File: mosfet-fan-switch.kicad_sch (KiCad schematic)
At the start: 21 parts, among them J1 12V IN, J2 PWM IN, J3 FAN OUT, Q1 irfz44n, Q2 2n7002, Q3 irf7416, U1 Arduino_Pro_Mini_3V3

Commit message: schematic + sim: NUC fan-header interface (PWM request divider, tach answer)
- J2 grown to 1x04 (Pro Mini), J4 added as the NUC's own 4-pin fan socket
- R7/R8 divider 10k/10k takes the NUC's 5 V PWM request down to the 3.3 V the
  Pro Mini expects; C5 1u + C6 100n filter it (tau 5.49 ms)
- R9 1k + Q4 (BC547) answer on the tach line as an open collector; the pull-up
  lives in the NUC (V4 + R10, both DNP)
- sim-only stand-ins V3/V4/V5, all DNP; connectors excluded from simulation
- fixed a pre-existing wiring bug: the old V2 -> R1 /PWM wire ran down U1's pin
  column and shorted D10-D13 to /PWM.  /PWM is D9 only.
- sim/nuc_link.py: duty table (2.500 V tap, 775 counts at 100 %, <=5 mV ripple),
  250 uA ITE load, tach levels, the legal 23-350 Hz carrier window
- sim/models/bc547.lib added and wired into the variant decks
- tools/fix_schematic_junctions.py restores junction dots that the KiCad MCP
  schematic edits silently delete
ERC: 0 errors, 0 warnings
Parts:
- removed J2: PWM IN, Connector_PinHeader_2.54mm:PinHeader_1x02_P2.54mm_Vertical, symbol Connector:Conn_01x02_Pin
- added C5: 1u, Capacitor_THT:CP_Radial_D8.0mm_P3.50mm, symbol Device:C
- added C6: 100n, Capacitor_THT:C_Disc_D3.8mm_W2.6mm_P2.50mm, symbol Device:C
- added J2: PRO MINI, Connector_PinHeader_2.54mm:PinHeader_1x04_P2.54mm_Vertical, symbol Connector_Generic:Conn_01x04
- added J4: NUC FAN HEADER, Connector_PinHeader_2.54mm:PinHeader_1x04_P2.54mm_Vertical, symbol Connector_Generic:Conn_01x04
- added Q4: BC547, Package_TO_SOT_THT:TO-92_Inline_Wide, symbol Transistor_BJT:BC547
- added R10: 1k, symbol Device:R
- added R7, R8: 10k, Resistor_THT:R_Axial_DIN0207_L6.3mm_D2.5mm_P7.62mm_Horizontal, symbol Device:R
- added R9: 1k, Resistor_THT:R_Axial_DIN0207_L6.3mm_D2.5mm_P7.62mm_Horizontal, symbol Device:R
- added V3, V5: VPULSE, symbol Simulation_SPICE:VPULSE
- added V4: 5, symbol Simulation_SPICE:VDC
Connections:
- net GND: now also C5.2, C6.2, J2.2 (Pin_2), J4.4 (Pin_4), Q4.3 (E), R8.2, V3.2, V4.2, V5.2
- net PWM: now also J2.1 (Pin_1)
- net TACH_PWM: now reaches U1.13 (D10)
- net TACH_PWM: now also J2.4 (Pin_4), R9.1, V5.1
- net DEMAND: now reaches U1.19 (A0)
- net DEMAND: now also C5.1, C6.1, J2.3 (Pin_3), R7.2, R8.1
- new net NUC_PWM: J4.1 (Pin_1), R7.1, V3.1
- new net NUC_TACH: J4.2 (Pin_2), Q4.1 (C), R10.1
- new net P5V: R10.2, V4.1
- new net TBASE: Q4.2 (B), R9.2
- no-connect marks 27 -> 26

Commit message: schematic: package-accurate transistor symbols; board stripped to a routing skeleton
The four transistors are now symbols whose pin numbers are the real leg numbers, so
KiCad's "symbol pin N <-> footprint pad N" rule puts every net on the correct leg and
Update PCB from Schematic agrees with the layout instead of fighting it.

- mosfet-fan-switch.kicad_sym + sym-lib-table: Q_NMOS_TO220 (1 gate, 2 drain, 3
  source), Q_NMOS_SOT23 (1 gate, 2 source, 3 drain), Q_PMOS_SO8 (1-3 source, 4 gate,
  5-8 drain), Q_NPN_TO92 (1 emitter, 2 base, 3 collector).  KiCad ships nothing like
  these: Transistor_BJT:BC547 extends Q_NPN_CBE (wrong for the flat-face TO-92) and
  there is no IRFZ44N symbol in any library at all.
- KiCad 10 ignores Sim.Pins for .model cards and writes every device line in symbol
  pin order, so the ngspice terminal order moved into .subckt wrappers in
  sim/models/*.lib:  XQ1 /GATE /DRAIN GND mos_irfz44n, XQ2 /LGATE GND /BOOT
  mos_2n7002, XQ3 /P12V x3 /BOOT /HIGATE x4 mos_irf7416, XQ4 GND /TBASE /NUC_TACH
  npn_bc547.  ngspice wants four nodes on a MOSFET card, so the bulk is spelled out
  and tied to the source inside each wrapper.
- sim/prepare_deck.py no longer repairs the NC-Q2-0 floating bulk (the three-pin
  SPICE symbols are gone); sim/variants.py and sim/nuc_link.py key the X cards and
  the pass-transistor variants now list nets in the chosen wrapper's own order.
  variants.csv is byte-identical to the pre-change baseline; fan_count.csv and
  nuc_link.csv differ only in timestep-sensitive averaged columns (supply average
  186.8 -> 187.2 mA, ITE load 40.3 -> 40.9 uA) - every DC and peak value identical.
- Q3 is drawn as the 8-pin package box, its legs tied by segmented wires with each
  node labelled once, moved east to (189.23, 170.18) so the 9.53 mm body clears the
  /BOOT branch at x=177.8.  ERC: 0 errors, 0 warnings.
- board: tools/skeleton_board.py removed the 63 generated tracks and kept all 26
  footprints, their positions and every pad's n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
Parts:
- Q1: symbol Simulation_SPICE:NMOS_Substrate -> mosfet-fan-switch:Q_NMOS_TO220
- Q2: symbol Simulation_SPICE:NMOS -> mosfet-fan-switch:Q_NMOS_SOT23
- Q3: symbol Simulation_SPICE:PMOS_Substrate -> mosfet-fan-switch:Q_PMOS_SO8
- Q4: symbol Transistor_BJT:BC547 -> mosfet-fan-switch:Q_NPN_TO92
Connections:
- net BOOT: now also Q2.3 (D), Q3.4 (G); no longer Q2.1 (D), Q3.2 (G)
- net DRAIN: now also Q1.2 (D); no longer Q1.1 (D)
- net GATE: now also Q1.1 (G); no longer Q1.2 (G)
- net GND: now also Q2.2 (S), Q4.1 (E); no longer Q1.4 (Bulk), Q2.3 (S), Q4.3 (E)
- net HIGATE: now also Q3.5 (D), Q3.6 (D), Q3.7 (D), Q3.8 (D); no longer Q3.1 (D)
- net LGATE: now also Q2.1 (G); no longer Q2.2 (G)
- net NUC_TACH: now also Q4.3 (C); no longer Q4.1 (C)
- net P12V: now also Q3.1 (S), Q3.2 (S); no longer Q3.4 (Bulk)
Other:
- note added: "PHYSICAL PINOUTS - symbols use package pin order: sheet numbers = board legs Q2 2N7002 SOT-23 1 gate /LGATE 2 source /GND 3 drain /BOOT Q3 IRF7416 SO-8 1,2,3 source /P12V 4 gate /BOOT 5..8 drain /HIGATE Q1 IRFZ44N TO-220 1 gate /GATE 2 drain /DRAIN 3 source /GND Q4 BC547 TO-92 1 emitter /GND 2 base /TBASE 3 collector /NUC_TACH D1 1N5819 DO-41 banded end (cathode) to +12 V, other end to /DRAIN J3 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"
- note removed: "PHYSICAL PINOUTS - the board follows the package, not the symbol's pin order Q2 2N7002 SOT-23 1 gate /LGATE 2 source /GND 3 drain /BOOT Q3 IRF7416 SO-8 1,2,3 source /P12V 4 gate /BOOT 5..8 drain /HIGATE Q1 IRFZ44N TO-220 1 gate /GATE 2 drain /DRAIN 3 source /GND D1 1N5819 DO-41 banded end (cathode) to +12 V, other end to /DRAIN J3 3 fans odd pins = +12 V, even pins = the switched /DRAIN side The 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"
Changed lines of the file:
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@@
 	)
 	(symbol
-		(lib_id "Simulation_SPICE:NMOS")
+		(lib_id "mosfet-fan-switch:Q_NMOS_SOT23")
 		(at 143.51 170.18 0)
 		(unit 1)
@@
 			)
 		)
-		(property "Sim.Name" "2n7002"
-			(at 143.51 170.18 0)
-			(effects
-				(font
-					(size 1.27 1.27)
-				)
-				(hide yes)
-			)
-		)
-		(property "Sim.Type" "VDMOS"
+		(property "Sim.Name" "mos_2n7002"
 			(at 143.51 170.18 0)
 			(effects
@@
 	)
 	(symbol
-		(lib_id "Simulation_SPICE:PMOS_Substrate")
-		(at 184.15 170.18 180)
+		(lib_id "mosfet-fan-switch:Q_PMOS_SO8")
+		(at 189.23 170.18 0)
 		(unit 1)
 		(body_style 1)
@@
 		(dnp no)
 		(property "Reference" "Q3"
-			(at 177.8 168.91 0)
+			(at 181.61 163.5 0)
 			(show_name no)
 			(do_not_autoplace no)
@@
 		)
 		(property "Value" "irf7416"
-			(at 177.8 171.45 0)
+			(at 186.69 177.8 0)
 			(show_name no)
 			(do_not_autoplace no)
@@
 		)
 		(property "Description" "P-channel MOSFET symbol with substrate (bulk) pin"
-			(at 184.15 170.18 0)
+			(at 189.23 170.18 0)
 			(hide yes)
 			(show_name no)
@@
 		)
 		(property "Sim.Library" "sim/models/irf7416.lib"
-			(at 184.15 170.18 0)
+			(at 189.23 170.18 0)
 			(effects
 				(font
@@
 			)
 		)
-		(property "Sim.Name" "irf7416"
-			(at 184.15 170.18 0)
-			(effects
-				(font
-					(size 1.27 1.27)
-				)
-				(hide yes)
-			)
-		)
-		(property "Sim.Type" "VDMOS"
-			(at 184.15 170.18 0)
+		(property "Sim.Name" "mos_irf7416"
+			(at 189.23 170.18 0)
 			(effects
 				(font
@@
 		(pin "4"
 		)
+		(pin "5"
+		)
+		(pin "6"
+		)
+		(pin "7"
+		)
+		(pin "8"
+		)
 		(instances
 			(project "mosfet-fan-switch"
@@
 	)
 	(symbol
-		(lib_id "Simulation_SPICE:NMOS_Substrate")
+		(lib_id "mosfet-fan-switch:Q_NMOS_TO220")
 		(at 224.79 190.5 0)
 		(unit 1)
@@
 			)
 		)
-		(property "Sim.Name" "irfz44n"
-			(at 224.79 190.5 0)
-			(effects
-				(font
-					(size 1.27 1.27)
-				)
-				(hide yes)
-			)
-		)
-		(property "Sim.Type" "VDMOS"
+		(property "Sim.Name" "mos_irfz44n"
 			(at 224.79 190.5 0)
 			(effects
@@
 		(pin "3"
 		)
-		(pin "4"
-		)
 		(instances
 			(project "mosfet-fan-switch"
@@
 	(wire
 		(pts
-			(xy 195.58 170.18) (xy 187.96 170.18)
+			(xy 195.58 170.18) (xy 193.04 170.18)
 		)
 		(stroke
@@
 	(wire
 		(pts
-			(xy 181.61 165.1) (xy 181.61 111.76)
-		)
-		(stroke
-			(width 0)
-			(type default)
-		)
-	)
-	(wire
-		(pts
-			(xy 179.07 165.1) (xy 181.61 165.1)
+			(xy 184.15 165.1) (xy 184.15 111.76)
 		)
 		(stroke
@@
 	(wire
 		(pts
-			(xy 227.32999999999998 195.58) (xy 229.87 195.58)
-		)
-		(stroke
-			(width 0)
-			(type default)
-		)
-	)
-	(wire
-		(pts
 			(xy 203.2 207.01) (xy 203.2 210.82)
 		)
@@
 	)
 	(label "BOOT"
-		(at 187.96 170.18 0)
-		(effects
-			(font
-				(size 1.27 1.27)
-			)
-			(justify left bottom)
-		)
-	)
-	(label "P12V"
-		(at 181.61 165.1 90)
+		(at 193.04 170.18 0)
 		(effects
 			(font
@@
 	)
 	(label "P12V"
-		(at 179.07 165.1 90)
+		(at 184.15 162.56 90)
 		(effects
 			(font
@@
 		)
 	)
-	(label "GND"
-		(at 229.87 195.58 270)
-		(effects
-			(font
-				(size 1.27 1.27)
-			)
-			(justify right bottom)
-		)
-	)
 	(label "P12V"
 		(at 241.3 148.59 90)
@@
 		)
 	)
-	(text "PHYSICAL PINOUTS - the board follows the package, not the symbol's pin order\nQ2  2N7002  SOT-23    1 gate /LGATE    2 source /GND     3 drain /BOOT\nQ3  IRF7416 SO-8      1,2,3 source /P12V   4 gate /BOOT   5..8 drain /HIGATE\nQ1  IRFZ44N TO-220    1 gate /GATE     2 drain /DRAIN    3 source /GND\nD1  1N5819  DO-41     banded end (cathode) to +12 V, other end to /DRAIN\nJ3  3 fans            odd pins = +12 V, even pins = the switched /DRAIN side\nThe SPICE symbols number MOSFET pins D-G-S, which is NOT the package order.\ndocs/pcb-notes.md carries the full pad-to-net table for the board."
+	(text "PHYSICAL PINOUTS - symbols use package pin order: sheet numbers = board legs\nQ2  2N7002  SOT-23    1 gate /LGATE    2 source /GND     3 drain /BOOT\nQ3  IRF7416 SO-8      1,2,3 source /P12V   4 gate /BOOT   5..8 drain /HIGATE\nQ1  IRFZ44N TO-220    1 gate /GATE     2 drain /DRAIN    3 source /GND\nQ4  BC547   TO-92     1 emitter /GND   2 base /TBASE     3 collector /NUC_TACH\nD1  1N5819  DO-41     banded end (cathode) to +12 V, other end to /DRAIN\nJ3  3 fans            odd pins = +12 V, even pins = the switched /DRAIN side\nngspice's own order (D-G-S-B, C-B-E) lives in the sim/models/ subckt wrappers\ndocs/pcb-notes.md carries the full pad-to-net table for the board."
 		(exclude_from_sim no)
 		(at 232 244 0)
@@
 	)
 	(junction
-		(at 138.43 170.18)
-		(diameter 0)
-		(color 0 0 0 0)
-	)
-	(junction
 		(at 138.43 210.82)
 		(diameter 0)
@@
 	)
 	(junction
-		(at 181.61 111.76)
-		(diameter 0)
-		(color 0 0 0 0)
-	)
-	(junction
-		(at 181.61 165.1)
+		(at 184.15 111.76)
 		(diameter 0)
 		(color 0 0 0 0)
@@
 	)
 	(junction
-		(at 227.33 195.58)
-		(diameter 0)
-		(color 0 0 0 0)
-	)
-	(junction
 		(at 227.33 210.82)
 		(diameter 0)
@@
 		(color 0 0 0 0)
 	)
-	(junction
-		(at 373.38 204.47)
-		(diameter 0)
-		(color 0 0 0 0)
-	)
 	(symbol
 		(lib_id "Simulation_SPICE:VPULSE")
@@
 	)
 	(symbol
-		(lib_id "Transistor_BJT:BC547")
+		(lib_id "mosfet-fan-switch:Q_NPN_TO92")
 		(at 378.46 204.47 0)
 		(unit 1)
@@
 			)
 		)
-		(property "Sim.Type" "GUMMELPOON"
-			(at 378.46 204.47 0)
-			(effects
-				(font
-					(size 1.27 1.27)
-				)
-				(hide yes)
-			)
-		)
-		(property "Sim.Name" "bc547"
+		(property "Sim.Name" "npn_bc547"
 			(at 378.46 204.47 0)
 			(effects
@@
 		)
 	)
+	(wire
+		(pts
+			(xy 184.15 165.1) (xy 186.69 165.1)
+		)
+		(stroke
+			(width 0)
+			(type default)
+		)
+	)
+	(wire
+		(pts
+			(xy 186.69 165.1) (xy 189.23 165.1)
+		)
+		(stroke
+			(width 0)
+			(type default)
+		)
+	)
+	(wire
+		(pts
+			(xy 181.61 175.26000000000002) (xy 184.15 175.26000000000002)
+		)
+		(stroke
+			(width 0)
+			(type default)
+		)
+	)
+	(wire
+		(pts
+			(xy 184.15 175.26000000000002) (xy 186.69 175.26000000000002)
+		)
+		(stroke
+			(width 0)
+			(type default)
+		)
+	)
+	(wire
+		(pts
+			(xy 186.69 175.26000000000002) (xy 189.23 175.26000000000002)
+		)
+		(stroke
+			(width 0)
+			(type default)
+		)
+	)

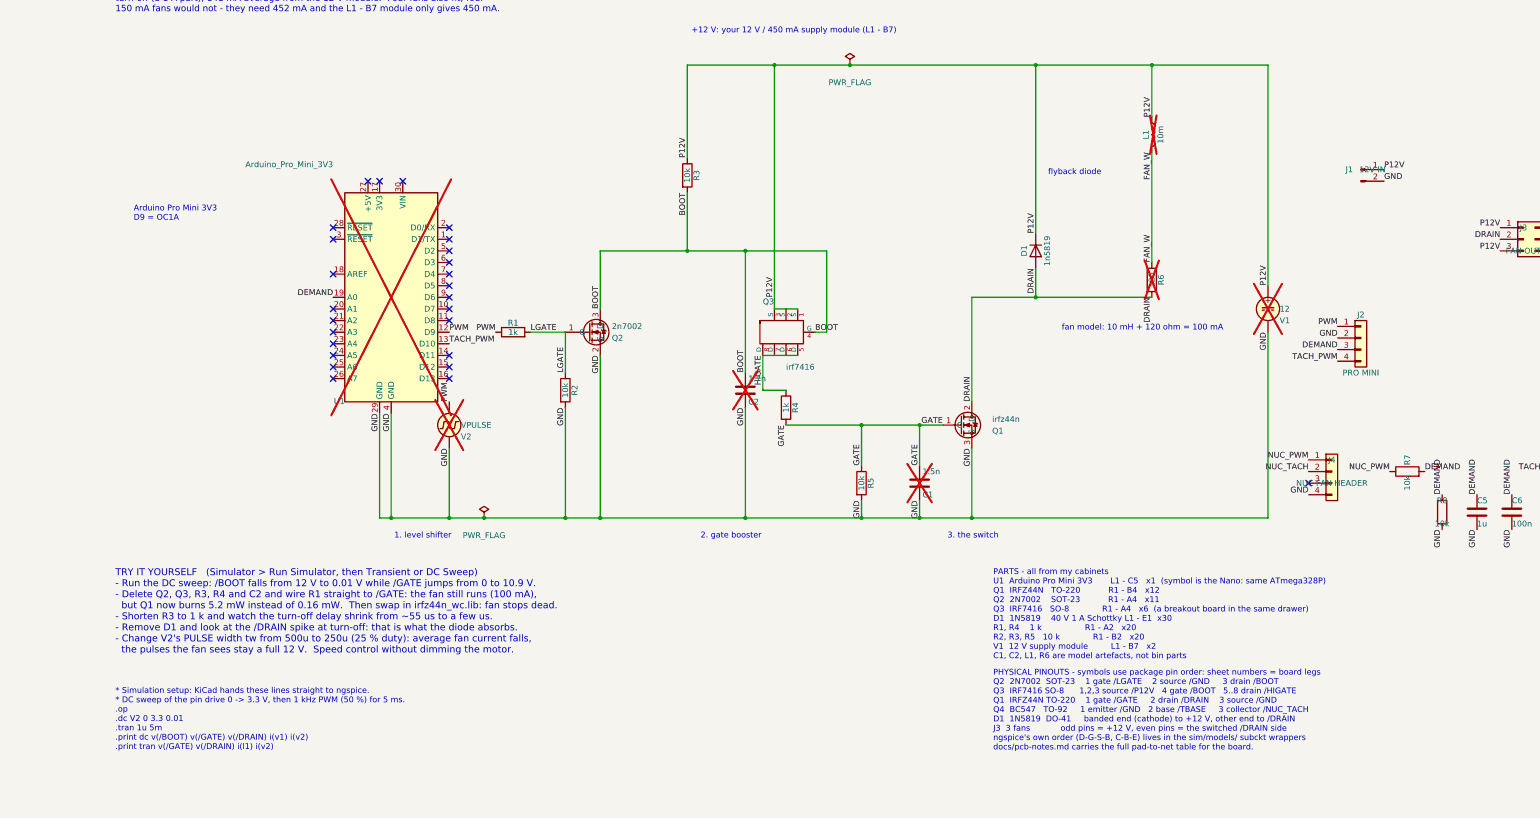
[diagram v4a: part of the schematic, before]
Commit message: sch: draw the Pro Mini itself, with its FTDI and ICSP headers
The Nano stand-in is gone.  U1 is now mosfet-fan-switch:Arduino_Pro_Mini_328,
generated from the same hole map as the board's socket footprint, so a symbol
pin number, a footprint pad number and the hole's silkscreen name are one
number.  J2 - the header that used to carry four signals to a module that was
not on the board - is deleted.

  * pcb/pro_mini.py now emits the symbol as well as the footprint.
  * tools/embed_pro_mini_schematic.py is the one-shot migration: it drops the
    Nano and J2 with their labels, no-connects and stubs, draws U1, J5 (FTDI
    row), J6 (2x3 ICSP, pin 2 deliberately dead), D2 and D3 (spare flyback
    diodes, unpopulated), and hands U1's programming-row GND to the GND rail.
  * KiCad only resolves symbols from the sheet's own lib_symbols cache, so the
    migration carries cached copies of everything it introduces.
  * Every new anchor sits on the 1.27 mm connection grid, which is what ERC's
    endpoint_off_grid check wants.
  * The board's footprints adopt the sheet's uuids, and D2/D3/J5/J6 now carry
    their real values.

ERC: 0 errors, 0 warnings.  DRC on the routing skeleton: no courtyard, silk,
clearance or hole violations; the same 7 cosmetic lib_footprint_mismatch
warnings and 68 expected unconnected pads.
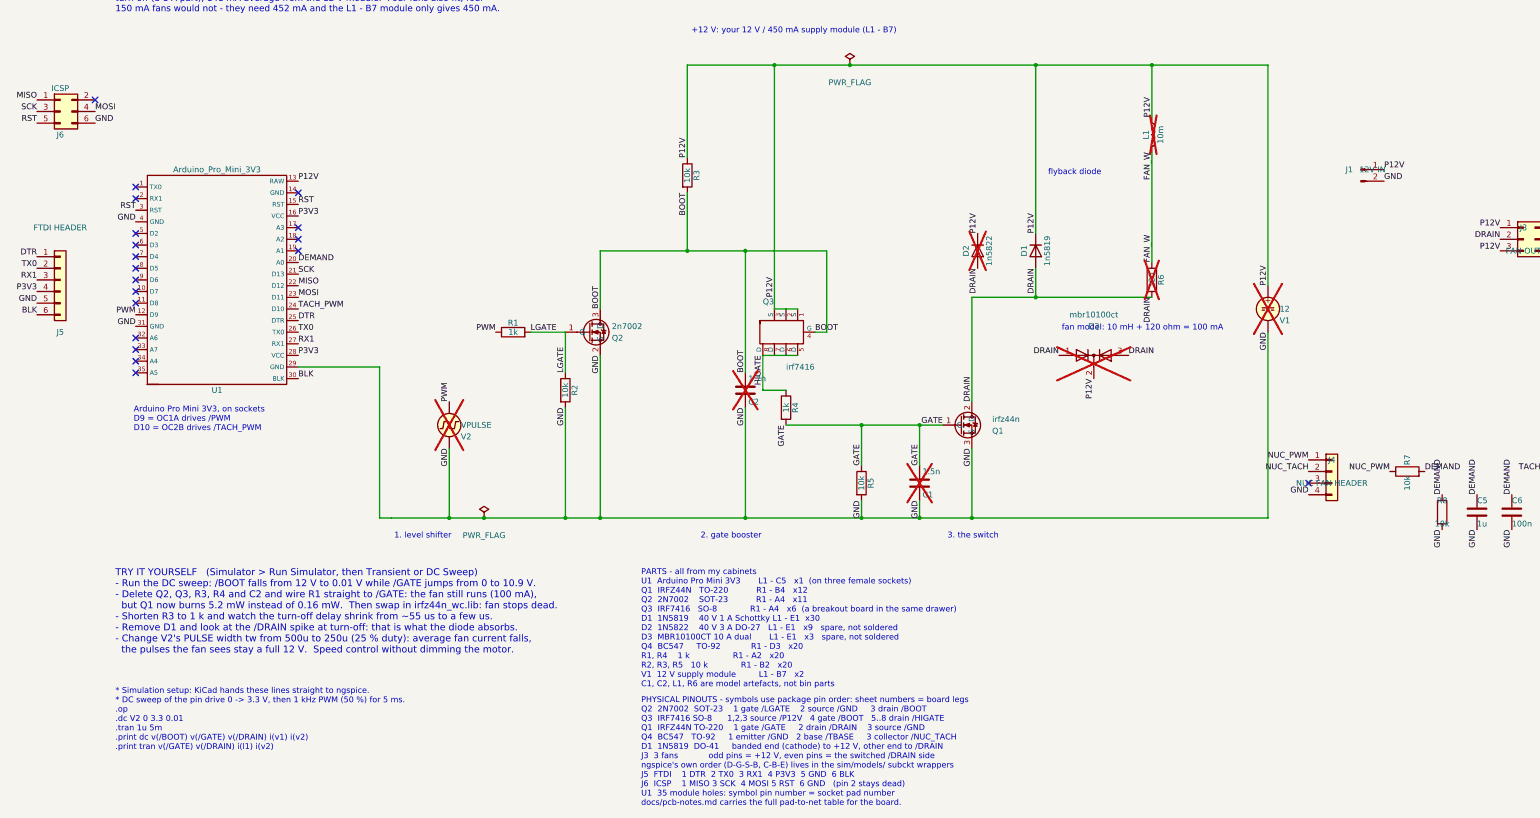
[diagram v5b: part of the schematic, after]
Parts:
- removed J2: PRO MINI, Connector_PinHeader_2.54mm:PinHeader_1x04_P2.54mm_Vertical, symbol Connector_Generic:Conn_01x04
- added D2: 1n5822, Diode_THT:D_DO-27_P15.24mm_Horizontal, symbol Device:D
- added D3: mbr10100ct, Package_TO_SOT_THT:TO-220-3_Vertical, symbol Device:D_Dual_CommonCathode_AKA
- added J5: FTDI HEADER, Connector_PinHeader_2.54mm:PinHeader_1x06_P2.54mm_Vertical, symbol Connector_Generic:Conn_01x06
- added J6: ICSP, Connector_PinHeader_2.54mm:PinHeader_2x03_P2.54mm_Vertical, symbol Connector_Generic:Conn_02x03_Odd_Even
- U1: footprint (none) -> mosfet-fan-switch:Arduino_Pro_Mini_328_Socket; symbol MCU_Module:Arduino_Nano_v2.x -> mosfet-fan-switch:Arduino_Pro_Mini_328; Note (none) -> the module sits on three female headers; measure its row sp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; now fitted
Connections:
- net DEMAND: now also U1.20 (A0); no longer U1.19 (A0)
- net DRAIN: now also D2.2 (A), D3.1 (A), D3.3 (A)
- net GND: now also U1.31 (GND), J5.5 (Pin_5), J6.6 (Pin_6)
- net P12V: now also U1.13 (RAW), D2.1 (K), D3.2 (K)
- net TACH_PWM: now also U1.24 (D10); no longer U1.13 (D10)
- net RST: now reaches U1.15 (RST)
- net RST: now also U1.3 (RST), J6.5 (Pin_5)
- net P3V3: now reaches U1.16 (VCC)
- net P3V3: now also U1.28 (VCC), J5.4 (Pin_4)
- net SCK: now reaches U1.21 (D13)
- net SCK: now also J6.3 (Pin_3)
- net MISO: now reaches U1.22 (D12)
- net MISO: now also J6.1 (Pin_1)
- net MOSI: now reaches U1.23 (D11)
- net MOSI: now also J6.4 (Pin_4)
- net DTR: now reaches U1.25 (DTR)
- net DTR: now also J5.1 (Pin_1)
- net TX0: now reaches U1.26 (TX0)
- net TX0: now also J5.2 (Pin_2)
- net RX1: now reaches U1.27 (RX1)
- net RX1: now also J5.3 (Pin_3)
- net BLK: now reaches U1.30 (BLK)
- net BLK: now also J5.6 (Pin_6)
- no-connect marks 26 -> 19
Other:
- note added: "Arduino Pro Mini 3V3, on sockets D9 = OC1A drives /PWM D10 = OC2B drives /TACH_PWM"
- note added: "PARTS - all from my cabinets U1 Arduino Pro Mini 3V3 L1 - C5 x1 (on three female sockets) Q1 IRFZ44N TO-220 R1 - B4 x12 Q2 2N7002 SOT-23 R1 - A4 x11 Q3 IRF7416 SO-8 R1 - A4 x6 (a breakout board in the same drawer) D1 1N5819 40 V 1 A Schottky L1 - E1 x30 D2 1N5822 40 V 3 A DO-27 L1 - E1 x9 spare, not soldered D3 MBR10100CT 10 A dual L1 - E1 x3 spare, not soldered Q4 BC547 TO-92 R1 - D3 x20 R1, R4 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"
- note removed: "Arduino Pro Mini 3V3 D9 = OC1A"
- note removed: "PARTS - all from my cabinets U1 Arduino Pro Mini 3V3 L1 - C5 x1 (symbol is the Nano: same ATmega328P) Q1 IRFZ44N TO-220 R1 - B4 x12 Q2 2N7002 SOT-23 R1 - A4 x11 Q3 IRF7416 SO-8 R1 - A4 x6 (a breakout board in the same drawer) D1 1N5819 40 V 1 A Schottky L1 - E1 x30 R1, R4 1 k R1 - A2 x20 R2, R3, R5 10 k R1 - B2 x20 V1 12 V supply module L1 - B7 x2 C1, C2, L1, R6 are model artefacts, not bin parts"
